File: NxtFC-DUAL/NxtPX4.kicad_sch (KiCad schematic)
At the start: 150 parts, among them J1 USB_C_Receptacle_USB2.0, J10 Micro_SD_Card, J11 Debug, J12 AuxGPIO, J2 DJIO3, J3 GPS, J4 UART2, J5 Upper computer connector, J6 ESC, J7 Upper computer connector, J8 PWM_AUX, J9 Conn_01x04, Q1 AP40P05, U1 MP9943GQ-Z, U10 Caution, U11 STM32H743VIH6, U13 SPL06, U14 BMI088, U15 BMI088, U16 W25Q128JVS, U17 UAV_LOGO, U19 SN74LVC1G86DCKR, U2 RT9013-33GB, U3 RT9013-33GB, U4 MP9943GQ-Z, U5 UAV_LOGO, U6 Direction_Logo, U8 Signature, U9 high_voltage, Y1 SG-210STF/ X1G004171002700, Y2 ABS07 (32.768kHZ)

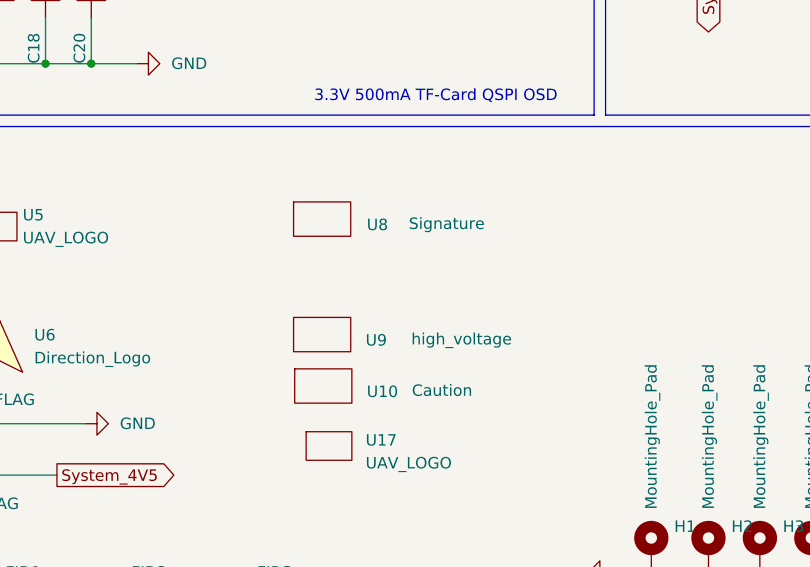
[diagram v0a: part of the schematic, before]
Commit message: [Rlease][Dual]: Update logo for Dual version
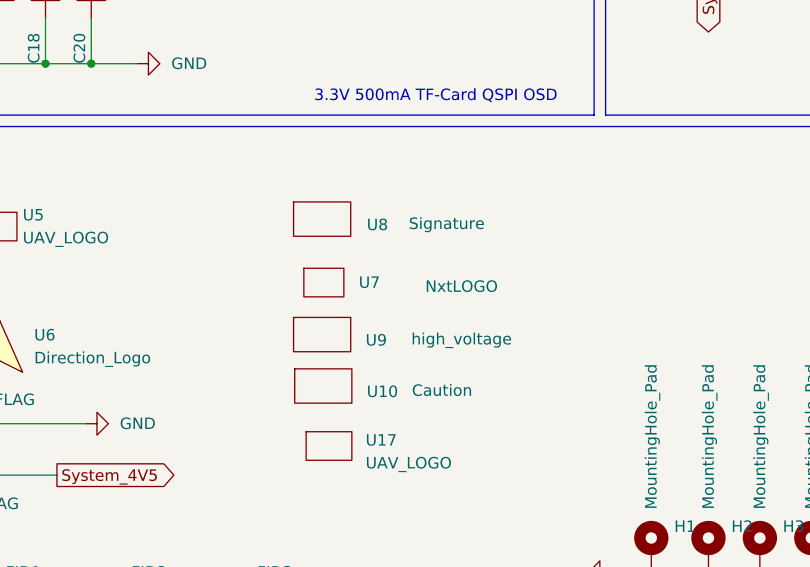
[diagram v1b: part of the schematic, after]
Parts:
- added U7: NxtLOGO, NxtPX4:NxtLOGO, symbol NxtPX4_Symbol:NxtLogo
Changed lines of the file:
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@@
+    )
+  )
+  (symbol (lib_id "NxtPX4_Symbol:NxtLogo") (at 175.768 299.212 0) (unit 1)
+    (in_bom yes) (on_board yes) (dnp no)
+    (property "Reference" "U7" (at 179.578 299.2755 0)
+      (effects (font (size 1.27 1.27)) (justify left))
+    )
+    (property "Value" "NxtLOGO" (at 191.008 299.72 0)
+      (effects (font (size 1.27 1.27)))
+    )
+    (property "Footprint" "NxtPX4:NxtLOGO" (at 176.276 303.53 0)
+      (effects (font (size 1.27 1.27)) hide)
+    )
+    (property "Datasheet" "" (at 175.768 299.212 0)
+      (effects (font (size 1.27 1.27)) hide)
+    )
+    (instances
+      (project "NxtPX4"
+        (path "/2d46c6c3-2f07-414b-a785-267d2b89c34b"
+          (reference "U7") (unit 1)
+        )
+      )
     )
   )
